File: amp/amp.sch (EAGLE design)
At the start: 69 parts, among them IC1 OPA2134PA, Q1 BC547, Q10 IRF510, Q11 BC556, Q12 BC556, Q13 BC547, Q14 BC547, Q15 2N7000, Q16 BC547, Q17 BC547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

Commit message: Back to 60V supply
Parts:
- R13, R24: value 3.3 -> 3.6
- R16, R3: value 20k -> 16k
- R21, R8: value 2.7k -> 2.2k
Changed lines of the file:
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@@
 <part name="Q2" library="my" deviceset="BC556" device=""/>
 <part name="Q4" library="my" deviceset="BC556" device=""/>
-<part name="R3" library="SparkFun-Resistors" deviceset="RESISTOR" device="PTH-1/4W" value="20k"/>
+<part name="R3" library="SparkFun-Resistors" deviceset="RESISTOR" device="PTH-1/4W" value="16k"/>
 <part name="R2" library="SparkFun-Resistors" deviceset="RESISTOR" device="PTH-1/4W" value="120"/>
 <part name="R5" library="SparkFun-Resistors" deviceset="RESISTOR" device="PTH-1/4W" value="120"/>
@@
 <part name="GND1" library="SparkFun-Aesthetics" deviceset="GND" device=""/>
 <part name="Q5" library="SparkFun-DiscreteSemi" deviceset="MOSFET-NCHANNEL" device="2N7000" value="2N7000"/>
-<part name="R8" library="SparkFun-Resistors" deviceset="RESISTOR" device="PTH-1/4W" value="2.7k"/>
+<part name="R8" library="SparkFun-Resistors" deviceset="RESISTOR" device="PTH-1/4W" value="2.2k"/>
 <part name="Q7" library="transistor-npn" deviceset="BC547*" device=""/>
 <part name="Q6" library="transistor-npn" deviceset="BC547*" device=""/>
@@
 <part name="Q10" library="my" deviceset="IRF510" device=""/>
 <part name="Q8" library="transistor-npn" deviceset="BC547*" device=""/>
-<part name="R13" library="SparkFun-Resistors" deviceset="RESISTOR" device="PTH-1/2W" value="3.3"/>
+<part name="R13" library="SparkFun-Resistors" deviceset="RESISTOR" device="PTH-1/2W" value="3.6"/>
 <part name="R12" library="SparkFun-Resistors" deviceset="RESISTOR" device="PTH-1/4W" value="10k"/>
 <part name="GND4" library="SparkFun-Aesthetics" deviceset="GND" device=""/>
@@
 <part name="Q11" library="my" deviceset="BC556" device=""/>
 <part name="Q12" library="my" deviceset="BC556" device=""/>
-<part name="R16" library="SparkFun-Resistors" deviceset="RESISTOR" device="PTH-1/4W" value="20k"/>
+<part name="R16" library="SparkFun-Resistors" deviceset="RESISTOR" device="PTH-1/4W" value="16k"/>
 <part name="R17" library="SparkFun-Resistors" deviceset="RESISTOR" device="PTH-1/4W" value="120"/>
 <part name="R18" library="SparkFun-Resistors" deviceset="RESISTOR" device="PTH-1/4W" value="120"/>
@@
 <part name="GND8" library="SparkFun-Aesthetics" deviceset="GND" device=""/>
 <part name="Q15" library="SparkFun-DiscreteSemi" deviceset="MOSFET-NCHANNEL" device="2N7000" value="2N7000"/>
-<part name="R21" library="SparkFun-Resistors" deviceset="RESISTOR" device="PTH-1/4W" value="2.7k"/>
+<part name="R21" library="SparkFun-Resistors" deviceset="RESISTOR" device="PTH-1/4W" value="2.2k"/>
 <part name="Q16" library="transistor-npn" deviceset="BC547*" device=""/>
 <part name="Q17" library="transistor-npn" deviceset="BC547*" device=""/>
@@
 <part name="Q19" library="my" deviceset="IRF510" device=""/>
 <part name="Q20" library="transistor-npn" deviceset="BC547*" device=""/>
-<part name="R24" library="SparkFun-Resistors" deviceset="RESISTOR" device="PTH-1/2W" value="3.3"/>
+<part name="R24" library="SparkFun-Resistors" deviceset="RESISTOR" device="PTH-1/2W" value="3.6"/>
 <part name="R25" library="SparkFun-Resistors" deviceset="RESISTOR" device="PTH-1/4W" value="10k"/>
 <part name="GND9" library="SparkFun-Aesthetics" deviceset="GND" device=""/>

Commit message: HV for neon bulb
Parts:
- V1, V2: value (none) -> 6922
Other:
- note added: "+10V"
- note added: "+60V"
- note added: "-10V"
- note added: "160mA"
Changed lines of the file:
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@@
 <parts>
 <part name="FRAME1" library="SparkFun-Aesthetics" deviceset="FRAME-A4L" device=""/>
-<part name="V1" library="tubes" deviceset="6922-P" device=""/>
+<part name="V1" library="tubes" deviceset="6922-P" device="" value="6922"/>
 <part name="Q2" library="my" deviceset="BC556" device=""/>
 <part name="Q4" library="my" deviceset="BC556" device=""/>
@@
 <part name="X5" library="con-wago-508" deviceset="W237-3E" device=""/>
 <part name="FRAME2" library="SparkFun-Aesthetics" deviceset="FRAME-A4L" device=""/>
-<part name="V2" library="tubes" deviceset="6922-P" device=""/>
+<part name="V2" library="tubes" deviceset="6922-P" device="" value="6922"/>
 <part name="Q11" library="my" deviceset="BC556" device=""/>
 <part name="Q12" library="my" deviceset="BC556" device=""/>
@@
 <sheet>
 <plain>
-<text x="48.26" y="76.2" size="1.778" layer="91">2mA</text>
-<text x="106.68" y="111.76" size="1.778" layer="91">20mA</text>
-<text x="162.56" y="114.3" size="1.778" layer="91">250mA</text>
-<text x="43.18" y="101.6" size="1.778" layer="91">1.3V</text>
+<text x="48.26" y="76.2" size="1.778" layer="97">2mA</text>
+<text x="106.68" y="104.14" size="1.778" layer="97">20mA</text>
+<text x="162.56" y="114.3" size="1.778" layer="97">160mA</text>
+<text x="43.18" y="101.6" size="1.778" layer="97">1.3V</text>
+<text x="50.8" y="172.72" size="1.778" layer="97">+60V</text>
+<text x="160.02" y="170.18" size="1.778" layer="97">+10V</text>
+<text x="160.02" y="88.9" size="1.778" layer="97">-10V</text>
+<text x="50.8" y="12.7" size="1.778" layer="97">-10V</text>
+<text x="114.3" y="88.9" size="1.778" layer="97">-10V</text>
+<text x="101.6" y="167.64" size="1.778" layer="97">+60V</text>
 </plain>
 <instances>

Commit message: Gate resistors added
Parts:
- added R33, R34: 100, SparkFun-Resistors:RESISTORPTH-1/4W
- Q10, Q18, Q19, Q9: value IRF510 -> IRF610; device my:IRF510 -> my:IRF610
- R27, R6: value 620 -> 2K
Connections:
- new net N$41: Q9.G, R33.1
- new net N$42: Q18.G, R34.1
- net N$13: now also R33.2; no longer Q9.G
- net N$31: now also R34.2; no longer Q18.G
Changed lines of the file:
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@@
 <part name="R9" library="SparkFun-Resistors" deviceset="RESISTOR" device="PTH-1/4W" value="120"/>
 <part name="R10" library="SparkFun-Resistors" deviceset="RESISTOR" device="PTH-1/4W" value="120"/>
-<part name="Q9" library="my" deviceset="IRF510" device=""/>
-<part name="Q10" library="my" deviceset="IRF510" device=""/>
+<part name="Q9" library="my" deviceset="IRF610" device=""/>
+<part name="Q10" library="my" deviceset="IRF610" device=""/>
 <part name="Q8" library="transistor-npn" deviceset="BC547*" device=""/>
 <part name="R13" library="SparkFun-Resistors" deviceset="RESISTOR" device="PTH-1/2W" value="3.6"/>
@@
 <part name="GND4" library="SparkFun-Aesthetics" deviceset="GND" device=""/>
 <part name="R7" library="SparkFun-Resistors" deviceset="RESISTOR" device="PTH-1/4W" value="10k"/>
-<part name="R6" library="SparkFun-Resistors" deviceset="RESISTOR" device="PTH-1/4W" value="620"/>
+<part name="R6" library="SparkFun-Resistors" deviceset="RESISTOR" device="PTH-1/4W" value="2K"/>
 <part name="GND2" library="SparkFun-Aesthetics" deviceset="GND" device=""/>
 <part name="IC1" library="linear" deviceset="OPA2*" device="PA" technology="134"/>
@@
 <part name="R22" library="SparkFun-Resistors" deviceset="RESISTOR" device="PTH-1/4W" value="120"/>
 <part name="R23" library="SparkFun-Resistors" deviceset="RESISTOR" device="PTH-1/4W" value="120"/>
-<part name="Q18" library="my" deviceset="IRF510" device=""/>
-<part name="Q19" library="my" deviceset="IRF510" device=""/>
+<part name="Q18" library="my" deviceset="IRF610" device=""/>
+<part name="Q19" library="my" deviceset="IRF610" device=""/>
 <part name="Q20" library="transistor-npn" deviceset="BC547*" device=""/>
 <part name="R24" library="SparkFun-Resistors" deviceset="RESISTOR" device="PTH-1/2W" value="3.6"/>
@@
 <part name="GND9" library="SparkFun-Aesthetics" deviceset="GND" device=""/>
 <part name="R26" library="SparkFun-Resistors" deviceset="RESISTOR" device="PTH-1/4W" value="10k"/>
-<part name="R27" library="SparkFun-Resistors" deviceset="RESISTOR" device="PTH-1/4W" value="620"/>
+<part name="R27" library="SparkFun-Resistors" deviceset="RESISTOR" device="PTH-1/4W" value="2K"/>
 <part name="GND10" library="SparkFun-Aesthetics" deviceset="GND" device=""/>
 <part name="R28" library="SparkFun-Resistors" deviceset="RESISTOR" device="PTH-1/4W" value="1M"/>
@@
 <part name="TP1" library="SparkFun-Passives" deviceset="TEST-POINT" device="TP_15TH_THRU"/>
 <part name="TP2" library="SparkFun-Passives" deviceset="TEST-POINT" device="TP_15TH_THRU"/>
+<part name="R33" library="SparkFun-Resistors" deviceset="RESISTOR" device="PTH-1/4W" value="100"/>
+<part name="R34" library="SparkFun-Resistors" deviceset="RESISTOR" device="PTH-1/4W" value="100"/>
 </parts>
 <sheets>
@@
 <instance part="R31" gate="R?" x="45.72" y="30.48" rot="R270"/>
 <instance part="TP2" gate="G$1" x="53.34" y="91.44"/>
+<instance part="R33" gate="G$1" x="139.7" y="152.4" rot="R180"/>
 </instances>
 <busses>
@@
 <wire x1="121.92" y1="134.62" x2="121.92" y2="152.4" width="0.1524" layer="91"/>
 <junction x="96.52" y="134.62"/>
-<pinref part="Q9" gate="G$1" pin="G"/>
-<wire x1="121.92" y1="152.4" x2="149.86" y2="152.4" width="0.1524" layer="91"/>
+<wire x1="121.92" y1="152.4" x2="134.62" y2="152.4" width="0.1524" layer="91"/>
+<pinref part="R33" gate="G$1" pin="2"/>
 </segment>
 </net>
@@
 <pinref part="R4" gate="G$1" pin="1"/>
 <wire x1="45.72" y1="35.56" x2="45.72" y2="40.64" width="0.1524" layer="91"/>
+</segment>
+</net>
+<net name="N$41" class="0">
+<segment>
+<pinref part="Q9" gate="G$1" pin="G"/>
+<pinref part="R33" gate="G$1" pin="1"/>
+<wire x1="144.78" y1="152.4" x2="149.86" y2="152.4" width="0.1524" layer="91"/>
 </segment>
 </net>
@@
 <instance part="R32" gate="R?" x="73.66" y="35.56" rot="R270"/>
 <instance part="TP1" gate="G$1" x="81.28" y="93.98"/>
+<instance part="R34" gate="G$1" x="167.64" y="157.48" rot="R180"/>
 </instances>
 <busses>
@@
 <wire x1="149.86" y1="139.7" x2="149.86" y2="157.48" width="0.1524" layer="91"/>
 <junction x="124.46" y="139.7"/>
-<pinref part="Q18" gate="G$1" pin="G"/>
-<wire x1="149.86" y1="157.48" x2="177.8" y2="157.48" width="0.1524" layer="91"/>
+<wire x1="149.86" y1="157.48" x2="162.56" y2="157.48" width="0.1524" layer="91"/>
+<pinref part="R34" gate="G$1" pin="2"/>
 </segment>
 </net>
@@
 </segment>
 </net>
+<net name="N$42" class="0">
+<segment>
+<pinref part="Q18" gate="G$1" pin="G"/>
+<pinref part="R34" gate="G$1" pin="1"/>
+<wire x1="172.72" y1="157.48" x2="177.8" y2="157.48" width="0.1524" layer="91"/>
+</segment>
+</net>

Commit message: Back to IRF5xx
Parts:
- Q10, Q18, Q19, Q9: value IRF610 -> IRF540; device my:IRF610 -> transistor-power:IRF540
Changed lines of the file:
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@@
 <part name="R9" library="SparkFun-Resistors" deviceset="RESISTOR" device="PTH-1/4W" value="120"/>
 <part name="R10" library="SparkFun-Resistors" deviceset="RESISTOR" device="PTH-1/4W" value="120"/>
-<part name="Q9" library="my" deviceset="IRF610" device=""/>
-<part name="Q10" library="my" deviceset="IRF610" device=""/>
+<part name="Q9" library="transistor-power" deviceset="IRF540" device=""/>
+<part name="Q10" library="transistor-power" deviceset="IRF540" device=""/>
 <part name="Q8" library="transistor-npn" deviceset="BC547*" device=""/>
 <part name="R13" library="SparkFun-Resistors" deviceset="RESISTOR" device="PTH-1/2W" value="3.6"/>
@@
 <part name="R22" library="SparkFun-Resistors" deviceset="RESISTOR" device="PTH-1/4W" value="120"/>
 <part name="R23" library="SparkFun-Resistors" deviceset="RESISTOR" device="PTH-1/4W" value="120"/>
-<part name="Q18" library="my" deviceset="IRF610" device=""/>
-<part name="Q19" library="my" deviceset="IRF610" device=""/>
+<part name="Q18" library="transistor-power" deviceset="IRF540" device=""/>
+<part name="Q19" library="transistor-power" deviceset="IRF540" device=""/>
 <part name="Q20" library="transistor-npn" deviceset="BC547*" device=""/>
 <part name="R24" library="SparkFun-Resistors" deviceset="RESISTOR" device="PTH-1/2W" value="3.6"/>

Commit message: HT filter added
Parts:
- Q16, Q17, Q6, Q7: value BC547 -> BC337; device transistor-npn:BC547 -> transistor:BC337
- R11, R30: value 430 -> 383
- R25: value 10k -> 4.7k
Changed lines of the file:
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@@
 <part name="Q5" library="SparkFun-DiscreteSemi" deviceset="MOSFET-NCHANNEL" device="2N7000" value="2N7000"/>
 <part name="R8" library="SparkFun-Resistors" deviceset="RESISTOR" device="PTH-1/4W" value="2.2k"/>
-<part name="Q7" library="transistor-npn" deviceset="BC547*" device=""/>
-<part name="Q6" library="transistor-npn" deviceset="BC547*" device=""/>
+<part name="Q7" library="transistor" deviceset="BC337" device=""/>
+<part name="Q6" library="transistor" deviceset="BC337" device=""/>
 <part name="R9" library="SparkFun-Resistors" deviceset="RESISTOR" device="PTH-1/4W" value="120"/>
 <part name="R10" library="SparkFun-Resistors" deviceset="RESISTOR" device="PTH-1/4W" value="120"/>
@@
 <part name="GND7" library="SparkFun-Aesthetics" deviceset="GND" device=""/>
 <part name="GND6" library="SparkFun-Aesthetics" deviceset="GND" device=""/>
-<part name="R11" library="SparkFun-Resistors" deviceset="RESISTOR" device="PTH-1/4W" value="430"/>
+<part name="R11" library="SparkFun-Resistors" deviceset="RESISTOR" device="PTH-1/4W" value="383"/>
 <part name="GND5" library="SparkFun-Aesthetics" deviceset="GND" device=""/>
 <part name="GND3" library="SparkFun-Aesthetics" deviceset="GND" device=""/>
@@
 <part name="Q15" library="SparkFun-DiscreteSemi" deviceset="MOSFET-NCHANNEL" device="2N7000" value="2N7000"/>
 <part name="R21" library="SparkFun-Resistors" deviceset="RESISTOR" device="PTH-1/4W" value="2.2k"/>
-<part name="Q16" library="transistor-npn" deviceset="BC547*" device=""/>
-<part name="Q17" library="transistor-npn" deviceset="BC547*" device=""/>
+<part name="Q16" library="transistor" deviceset="BC337" device=""/>
+<part name="Q17" library="transistor" deviceset="BC337" device=""/>
 <part name="R22" library="SparkFun-Resistors" deviceset="RESISTOR" device="PTH-1/4W" value="120"/>
 <part name="R23" library="SparkFun-Resistors" deviceset="RESISTOR" device="PTH-1/4W" value="120"/>
@@
 <part name="Q20" library="transistor-npn" deviceset="BC547*" device=""/>
 <part name="R24" library="SparkFun-Resistors" deviceset="RESISTOR" device="PTH-1/2W" value="3.6"/>
-<part name="R25" library="SparkFun-Resistors" deviceset="RESISTOR" device="PTH-1/4W" value="10k"/>
+<part name="R25" library="SparkFun-Resistors" deviceset="RESISTOR" device="PTH-1/4W" value="4.7k"/>
 <part name="GND9" library="SparkFun-Aesthetics" deviceset="GND" device=""/>
 <part name="R26" library="SparkFun-Resistors" deviceset="RESISTOR" device="PTH-1/4W" value="10k"/>
@@
 <part name="GND11" library="SparkFun-Aesthetics" deviceset="GND" device=""/>
 <part name="GND12" library="SparkFun-Aesthetics" deviceset="GND" device=""/>
-<part name="R30" library="SparkFun-Resistors" deviceset="RESISTOR" device="PTH-1/4W" value="430"/>
+<part name="R30" library="SparkFun-Resistors" deviceset="RESISTOR" device="PTH-1/4W" value="383"/>
 <part name="LOGO1" library="my" deviceset="LOGO-MANTIS" device=""/>
 <part name="R31" library="SparkFun-Electromechanical" deviceset="TRIMPOT" device="3362U-2" value="500"/>

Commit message: More tweaks
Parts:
- R13, R24: value 3.6 -> 2.4
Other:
- note removed: "160mA"
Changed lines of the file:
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@@
 <part name="Q10" library="transistor-power" deviceset="IRF540" device=""/>
 <part name="Q8" library="transistor-npn" deviceset="BC547*" device=""/>
-<part name="R13" library="SparkFun-Resistors" deviceset="RESISTOR" device="PTH-1/2W" value="3.6"/>
+<part name="R13" library="SparkFun-Resistors" deviceset="RESISTOR" device="PTH-1/2W" value="2.4"/>
 <part name="R12" library="SparkFun-Resistors" deviceset="RESISTOR" device="PTH-1/4W" value="10k"/>
 <part name="GND4" library="SparkFun-Aesthetics" deviceset="GND" device=""/>
@@
 <part name="Q19" library="transistor-power" deviceset="IRF540" device=""/>
 <part name="Q20" library="transistor-npn" deviceset="BC547*" device=""/>
-<part name="R24" library="SparkFun-Resistors" deviceset="RESISTOR" device="PTH-1/2W" value="3.6"/>
+<part name="R24" library="SparkFun-Resistors" deviceset="RESISTOR" device="PTH-1/2W" value="2.4"/>
 <part name="R25" library="SparkFun-Resistors" deviceset="RESISTOR" device="PTH-1/4W" value="4.7k"/>
 <part name="GND9" library="SparkFun-Aesthetics" deviceset="GND" device=""/>
@@
 <text x="48.26" y="76.2" size="1.778" layer="97">2mA</text>
 <text x="106.68" y="104.14" size="1.778" layer="97">20mA</text>
-<text x="162.56" y="114.3" size="1.778" layer="97">160mA</text>
+<text x="162.56" y="114.3" size="1.778" layer="97">250mA</text>
 <text x="43.18" y="101.6" size="1.778" layer="97">1.3V</text>
 <text x="50.8" y="172.72" size="1.778" layer="97">+60V</text>
@@
 <plain>
 <text x="76.2" y="81.28" size="1.778" layer="91">2mA</text>
-<text x="134.62" y="116.84" size="1.778" layer="91">20mA</text>
-<text x="190.5" y="119.38" size="1.778" layer="91">250mA</text>
+<text x="134.62" y="116.84" size="1.778" layer="97">20mA</text>
+<text x="190.5" y="119.38" size="1.778" layer="97">250mA</text>
 <text x="71.12" y="106.68" size="1.778" layer="91">1.3V</text>
 </plain>

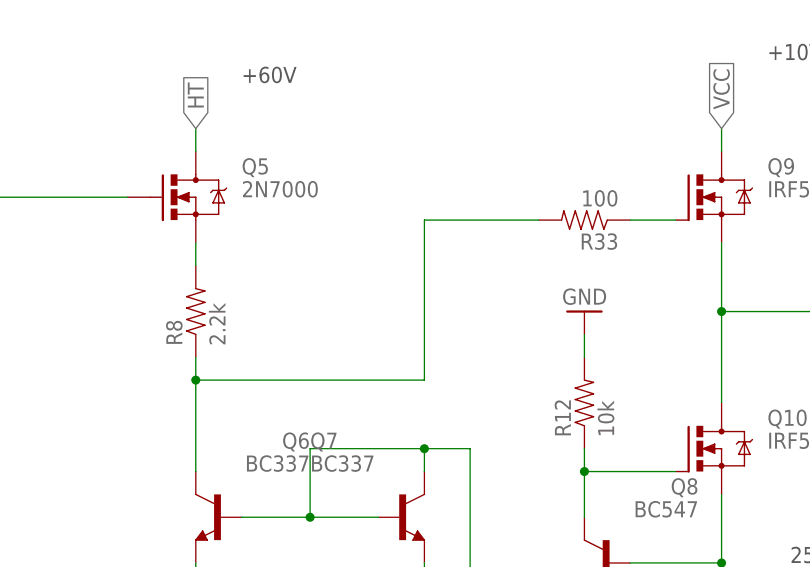
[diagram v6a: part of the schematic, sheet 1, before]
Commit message: Small bypass cap added
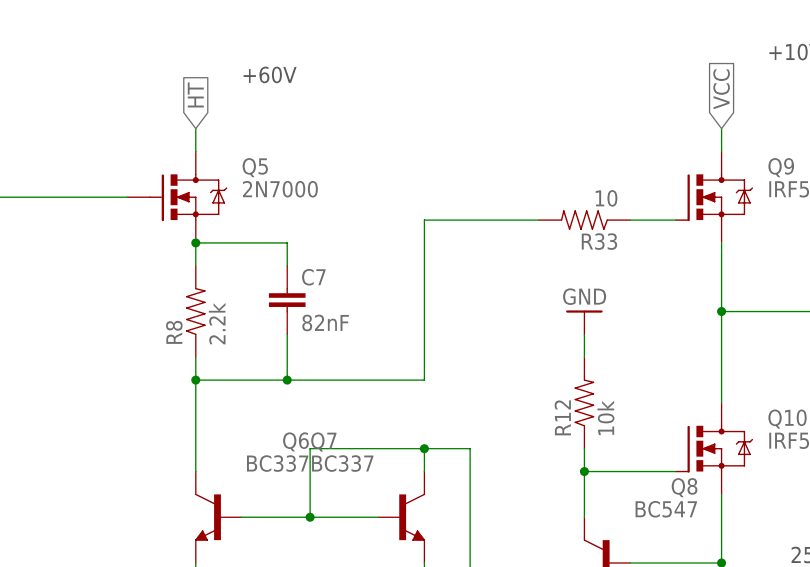
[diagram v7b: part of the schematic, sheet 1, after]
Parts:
- added C7, C8: 82nF, SparkFun-Capacitors:1.0UF-25V-+80/-20(0805)"
- R33, R34: value 100 -> 10
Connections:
- net N$13: now also C7.2
- net N$14: now also C7.1
- net N$31: now also C8.2
- net N$32: now also C8.1
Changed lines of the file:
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@@
 <part name="TP1" library="SparkFun-Passives" deviceset="TEST-POINT" device="TP_15TH_THRU"/>
 <part name="TP2" library="SparkFun-Passives" deviceset="TEST-POINT" device="TP_15TH_THRU"/>
-<part name="R33" library="SparkFun-Resistors" deviceset="RESISTOR" device="PTH-1/4W" value="100"/>
-<part name="R34" library="SparkFun-Resistors" deviceset="RESISTOR" device="PTH-1/4W" value="100"/>
+<part name="R33" library="SparkFun-Resistors" deviceset="RESISTOR" device="PTH-1/4W" value="10"/>
+<part name="R34" library="SparkFun-Resistors" deviceset="RESISTOR" device="PTH-1/4W" value="10"/>
+<part name="C7" library="SparkFun-Capacitors" deviceset="1.0UF-25V-+80/-20(0805)" device="&quot;" value="82nF"/>
+<part name="C8" library="SparkFun-Capacitors" deviceset="1.0UF-25V-+80/-20(0805)" device="&quot;" value="82nF"/>
 </parts>
 <sheets>
@@
 <instance part="TP2" gate="G$1" x="53.34" y="91.44"/>
 <instance part="R33" gate="G$1" x="139.7" y="152.4" rot="R180"/>
+<instance part="C7" gate="G$1" x="106.68" y="142.24"/>
 </instances>
 <busses>
@@
 <wire x1="96.52" y1="124.46" x2="96.52" y2="134.62" width="0.1524" layer="91"/>
 <wire x1="96.52" y1="134.62" x2="96.52" y2="137.16" width="0.1524" layer="91"/>
-<wire x1="96.52" y1="134.62" x2="121.92" y2="134.62" width="0.1524" layer="91"/>
+<wire x1="96.52" y1="134.62" x2="106.68" y2="134.62" width="0.1524" layer="91"/>
+<wire x1="106.68" y1="134.62" x2="121.92" y2="134.62" width="0.1524" layer="91"/>
 <wire x1="121.92" y1="134.62" x2="121.92" y2="152.4" width="0.1524" layer="91"/>
 <junction x="96.52" y="134.62"/>
 <wire x1="121.92" y1="152.4" x2="134.62" y2="152.4" width="0.1524" layer="91"/>
 <pinref part="R33" gate="G$1" pin="2"/>
+<pinref part="C7" gate="G$1" pin="2"/>
+<wire x1="106.68" y1="139.7" x2="106.68" y2="134.62" width="0.1524" layer="91"/>
+<junction x="106.68" y="134.62"/>
 </segment>
 </net>
@@
 <pinref part="Q5" gate="G$1" pin="S"/>
 <wire x1="96.52" y1="147.32" x2="96.52" y2="149.86" width="0.1524" layer="91"/>
+<pinref part="C7" gate="G$1" pin="1"/>
+<wire x1="106.68" y1="147.32" x2="106.68" y2="149.86" width="0.1524" layer="91"/>
+<wire x1="106.68" y1="149.86" x2="96.52" y2="149.86" width="0.1524" layer="91"/>
+<junction x="96.52" y="149.86"/>
 </segment>
 </net>
@@
 <instance part="TP1" gate="G$1" x="81.28" y="93.98"/>
 <instance part="R34" gate="G$1" x="167.64" y="157.48" rot="R180"/>
+<instance part="C8" gate="G$1" x="134.62" y="147.32"/>
 </instances>
 <busses>
@@
 <wire x1="124.46" y1="129.54" x2="124.46" y2="139.7" width="0.1524" layer="91"/>
 <wire x1="124.46" y1="139.7" x2="124.46" y2="142.24" width="0.1524" layer="91"/>
-<wire x1="124.46" y1="139.7" x2="149.86" y2="139.7" width="0.1524" layer="91"/>
+<wire x1="124.46" y1="139.7" x2="134.62" y2="139.7" width="0.1524" layer="91"/>
+<wire x1="134.62" y1="139.7" x2="149.86" y2="139.7" width="0.1524" layer="91"/>
 <wire x1="149.86" y1="139.7" x2="149.86" y2="157.48" width="0.1524" layer="91"/>
 <junction x="124.46" y="139.7"/>
 <wire x1="149.86" y1="157.48" x2="162.56" y2="157.48" width="0.1524" layer="91"/>
 <pinref part="R34" gate="G$1" pin="2"/>
+<pinref part="C8" gate="G$1" pin="2"/>
+<wire x1="134.62" y1="144.78" x2="134.62" y2="139.7" width="0.1524" layer="91"/>
+<junction x="134.62" y="139.7"/>
 </segment>
 </net>
@@
 <pinref part="Q15" gate="G$1" pin="S"/>
 <wire x1="124.46" y1="152.4" x2="124.46" y2="154.94" width="0.1524" layer="91"/>
-</segment>
-</net>
+<pinref part="C8" gate="G$1" pin="1"/>
+<wire x1="134.62" y1="152.4" x2="134.62" y2="154.94" width="0.1524" layer="91"/>
+<wire x1="134.62" y1="154.94" x2="124.46" y2="154.94" width="0.1524" layer="91"/>
+<junction x="124.46" y="154.94"/>
+</segment>
+</net>
